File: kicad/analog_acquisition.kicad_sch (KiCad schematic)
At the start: 65 parts, among them J2 BNC_Isolated, J3 BNC_Isolated, J4 JST-XH 3-pin, J5 BNC_Isolated, J6 JST-XH 2-pin, J7 JST-XH 3-pin, T1 Transformer_SP_2S, T2 Transformer_SP_2S, T3 Transformer_SP_2S, U10 MCP6002, U11 MCP6002, U12 SN6501, U13 AMC1301, U4 MCP6002, U5 SN6501, U6 AMC1301, U7 MCP6002, U8 SN6501, U9 AMC1301

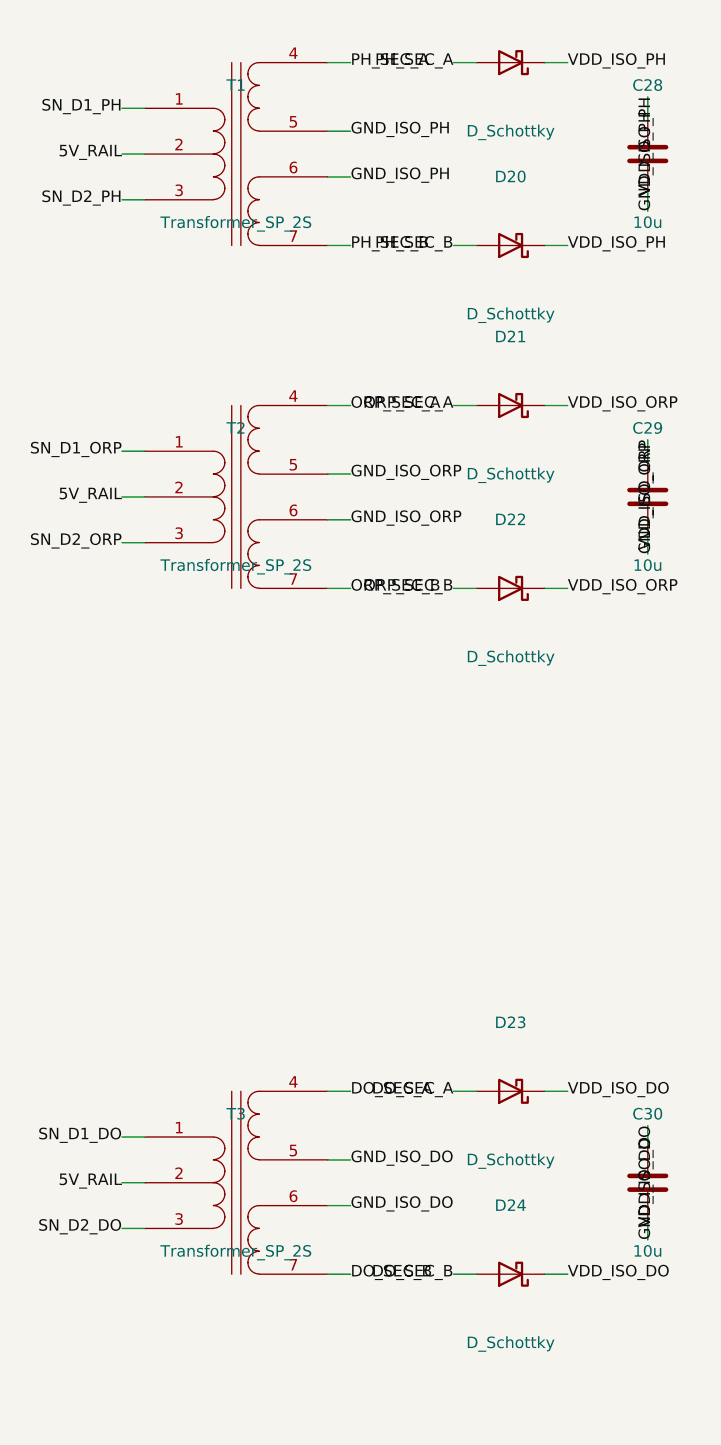
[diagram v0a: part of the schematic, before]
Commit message: fix(sch,pcb): Fase 3 — reparar nets críticas y paridad T1/T2/T3
- Corrige conexiones secundarias de T1/T2/T3: *_SEC_B pasa del pin 7 al
  pin 6 del footprint Wuerth 750315371 (6 pads); pin 7 no-conectado.
  *_SEC_A en pin 4, GND_ISO_* en pin 5.
- Actualiza pad nets en PCB para T1/T2/T3 según netlist corregido.
- Marca items de Fase 3 completados en la bitácora.
- tools/compare_pcb_to_netlist.py: ignora pines con pintype no_connect y
  nets 'unconnected-' para evitar falsos positivos de paridad.

ERC: 0 violaciones. DRC error-level: 0 violaciones, 394 desconectados
baseline. Paridad esquemático/PCB: 0 problemas.

Co-Authored-By: Devin AI <158243242+devin-ai-integration[bot]@users.noreply.github.com>
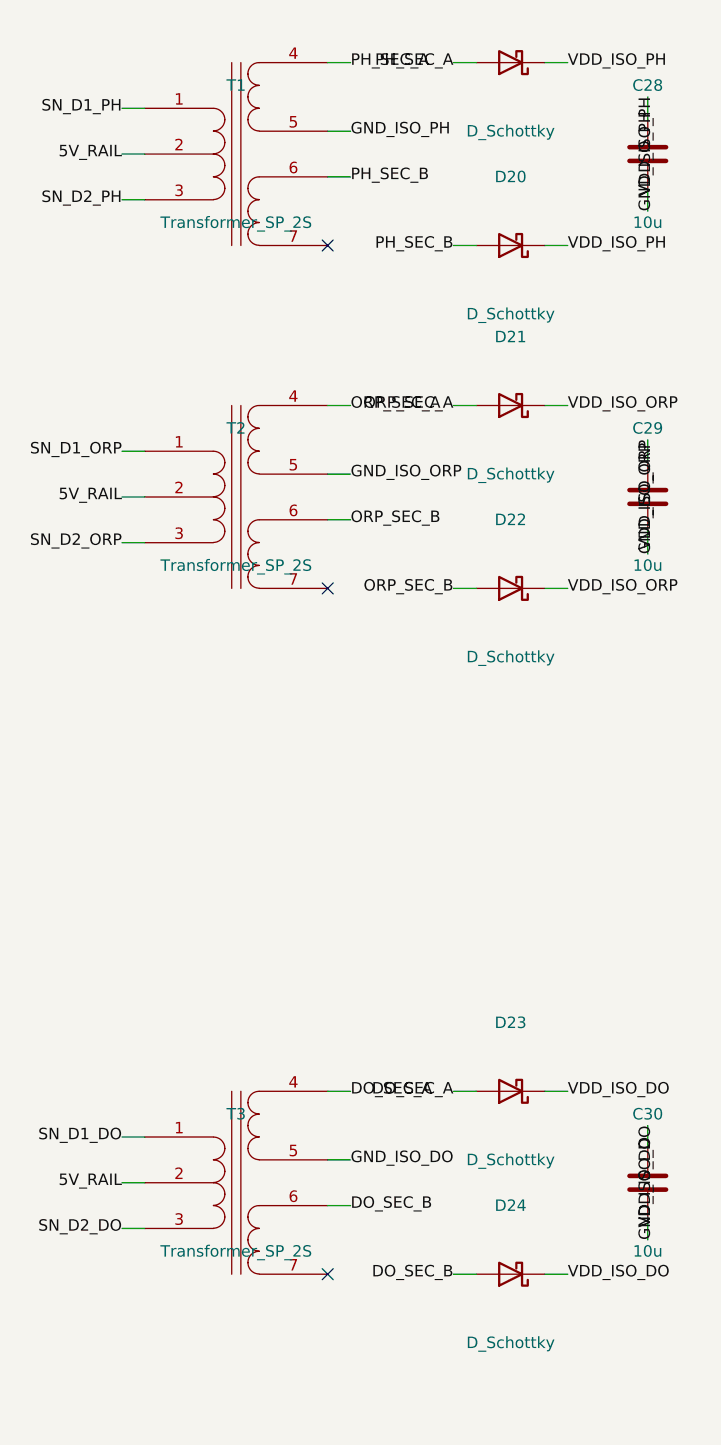
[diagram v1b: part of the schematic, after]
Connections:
- net DO_SEC_B: now also T3.6 (OUT2A); no longer T3.7 (OUT2B)
- net GND_ISO_DO: no longer T3.6 (OUT2A)
- net GND_ISO_ORP: no longer T2.6 (OUT2A)
- net GND_ISO_PH: no longer T1.6 (OUT2A)
- net ORP_SEC_B: now also T2.6 (OUT2A); no longer T2.7 (OUT2B)
- net PH_SEC_B: now also T1.6 (OUT2A); no longer T1.7 (OUT2B)
- no-connect marks 10 -> 13
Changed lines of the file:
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@@
     (effects (font (size 1.27 1.27)))
   )
-  (wire (pts (xy 254.0 73.66) (xy 256.54 73.66))
-    (stroke (width 0) (type default))
-  )
-  (label "PH_SEC_B" (at 256.54 73.66 0)
-    (effects (font (size 1.27 1.27)))
-  )
+  (no_connect (at 254.0 73.66))
   (wire (pts (xy 254.0 60.96) (xy 256.54 60.96))
     (stroke (width 0) (type default))
@@
     (stroke (width 0) (type default))
   )
-  (label "GND_ISO_PH" (at 256.54 66.04 0)
+  (label "PH_SEC_B" (at 256.54 66.04 0)
     (effects (font (size 1.27 1.27)))
   )
@@
     (effects (font (size 1.27 1.27)))
   )
-  (wire (pts (xy 254.0 111.76) (xy 256.54 111.76))
-    (stroke (width 0) (type default))
-  )
-  (label "ORP_SEC_B" (at 256.54 111.76 0)
-    (effects (font (size 1.27 1.27)))
-  )
+  (no_connect (at 254.0 111.76))
   (wire (pts (xy 254.0 99.06) (xy 256.54 99.06))
     (stroke (width 0) (type default))
@@
     (stroke (width 0) (type default))
   )
-  (label "GND_ISO_ORP" (at 256.54 104.14 0)
+  (label "ORP_SEC_B" (at 256.54 104.14 0)
     (effects (font (size 1.27 1.27)))
   )
@@
     (effects (font (size 1.27 1.27)))
   )
-  (wire (pts (xy 254.0 187.96) (xy 256.54 187.96))
-    (stroke (width 0) (type default))
-  )
-  (label "DO_SEC_B" (at 256.54 187.96 0)
-    (effects (font (size 1.27 1.27)))
-  )
+  (no_connect (at 254.0 187.96))
   (wire (pts (xy 254.0 175.26) (xy 256.54 175.26))
     (stroke (width 0) (type default))
@@
     (stroke (width 0) (type default))
   )
-  (label "GND_ISO_DO" (at 256.54 180.34 0)
-    (effects (font (size 1.27 1.27)))
-  )
+  (label "DO_SEC_B" (at 256.54 180.34 0)
+    (effects (font (size 1.27 1.27)))
+  )

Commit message: feat(sch,pcb,docs): redefine tiers Essential/Insight/Signature and sync DNP
- Tier mapping:
  - Essential: GPS, RTC/timestamp, temperature, pH, ORP
  - Insight: Essential + CO2 pressure (A4), DO (A5), HX711 load cell,
    chiller, recirculation motor, gas solenoid (single gas via K1/J18)
  - Signature: Insight + Hamilton TCD + ACD via RS485 bridge
- Humidity channel (J7/D8/R17/R18/C23) and PWM gas valve (U20/Q5/D14/R28/C27/J22)
  marked DNP in all tiers.
- Update DNP properties in kicad/analog_acquisition.kicad_sch,
  kicad/digital_i2c.kicad_sch, kicad/actuator_drivers.kicad_sch,
  kicad/power_management.kicad_sch using kicad/tier_dnp_mapping.json.
- Update sheet comments and root text block.
- Update docs/04_BOM_PRODUCTION.md section 11, docs/INSIGHT_FABRICATION_ROADMAP.md,
  and docs/DOCUMENTATION_UPDATE_AUDIT.md.
- Add helper tools: build_tier_map.py, apply_tier_dnp4.py, update_tier_comments.py,
  list_actual_components.py, tier_counts.py, validate_sch.py, count_parens.py.
- Sync current PCB state (component positions/nets) to match corrected netlist.

Validation:
- kicad-cli sch erc --severity-all: 0 violaciones
- kicad-cli pcb drc --severity-error: 0 violaciones, 332 unconnected items
- compare_pcb_to_netlist.py: 0 parity problems

Co-Authored-By: Devin AI <158243242+devin-ai-integration[bot]@users.noreply.github.com>
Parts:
- C12, C13, C14, C15, C16, C17, C22, C24, C28, C29, D19, D20, D21, D22, D3, D4, D7, R10, R15, R16, R30, R31, R32, R33, R7, R8, R9, T1, T2, TP1, TP2, U4, U5, U6, U7, U8, U9: DNP (none) -> NO
- C18, C19, C20, C21, C30, D23, D24, D5, D6, R11, R12, R13, R14, T3, U10, U11, U12, U13: DNP (none) -> Essential
- C23, D8, R17, R18: DNP (none) -> Essential,Insight,Signature
- J4, J5: DNP Insight+ -> Essential
- J7: DNP Signature -> Essential,Insight,Signature
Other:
- note added: "ANALOG ACQUISITION — 5 active channels with on-board galvanic isolation Wet sensors (pH, ORP, DO) use dedicated SN6501 isolation barrier Channels: pH(A0), ORP(A1), Temp(A2), CO2(A4), DO(A5); HUM(A3) removed/DNP All channels: Connector → TVS ESD → RC filter → Op-amp buffer → ADC Pull-downs 10M prevent floating reads when sensor disconnected"
- note added: "CO2 Channel (A4) — Tier: Insight+ JST-XH — transductor presión CO₂"
- note added: "DO Channel (A5) — Tier: Insight+ BNC hembra — sonda DO"
- note added: "HUM Channel (A3) — Tier: removed/DNP all tiers J7 + D8 + R17/R18/C23 not populated"
- note added: "TEMP Channel (A2) — Tier: Essential+ JST-XH — NTC thermistor"
- note removed: "ANALOG ACQUISITION — 6 channels with on-board galvanic isolation Each wet sensor (pH, ORP, DO) has dedicated SN6501+ADuM1250 isolation barrier All channels: Connector → TVS ESD → RC filter → Op-amp buffer → ADC Pull-downs 10M prevent floating reads when sensor disconnected"
- note removed: "CO2 Channel (A2) — Tier: Insight+ JST-XH — transductor presión CO₂"
- note removed: "DO Channel (A3) — Tier: Insight+ BNC hembra — sonda DO"
- note removed: "HUM Channel (A5) — Tier: Signature JST-XH — sensor humedad"
- note removed: "TEMP Channel (A4) — Tier: Essential+ JST-XH — NTC thermistor"
